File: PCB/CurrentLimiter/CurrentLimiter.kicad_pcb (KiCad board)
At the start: 2 copper layers, 24 parts, among them P1 Signals, P2 OpAmp1-4, P3 OpAmp5-8, Q1 Q_PMOS_GSD, Q2 Q_NPN_BEC, Q3 Q_NPN_BEC, Q4 Q_NPN_BEC, U1 LM358

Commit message: Overcurrent protection proto PCB mostly done
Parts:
- P1: footprint Pin_Headers:Pin_Header_Straight_1x06_Pitch2.54mm -> Pin_Headers:Pin_Header_Straight_1x07_Pitch2.54mm
- moved D1 47.0 mm to (152.0, 129.5), turned to 180 degrees
- moved R6 46.3 mm to (145.4, 115.0), turned to 270 degrees
- moved R5 45.4 mm to (146.7, 128.3), turned to 180 degrees
- moved Q4 42.4 mm to (142.9, 120.7), turned to 90 degrees
- moved R4 35.7 mm to (151.8, 127.0), turned to 180 degrees
- moved R11 32.4 mm to (170.1, 116.8), turned to 180 degrees
- moved R1 30.4 mm to (163.3, 128.6), turned to 180 degrees
- moved W2 30.0 mm to (142.2, 114.9)
- moved R3 29.7 mm to (146.6, 125.1), turned to 180 degrees
- moved R2 28.8 mm to (151.8, 123.8), turned to 180 degrees
- moved R9 28.0 mm to (168.9, 113.0), turned to 90 degrees
- moved P1 26.0 mm to (155.6, 132.7), turned to 90 degrees
- moved Q2 24.2 mm to (157.7, 128.9)
- moved W1 23.2 mm to (158.1, 125.1)
- moved Q3 22.3 mm to (146.4, 120.7), turned to 270 degrees
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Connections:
- P1 pad 1: +12V -> Vref
- P1 pad 3: Vref -> GND
- P1 pad 4: V- -> +12V
- P1 pad 5: V+ -> Vout
- P1 pad 6: GND -> V+
- Q1 pad 3: Net-(Q1-Pad3) -> Vout
- R2 pad 1: Net-(Q1-Pad3) -> Vout
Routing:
- net GND: track 0.00 -> 73.1 mm, vias 0 -> 2
- net Vref: track 4.25 -> 60.3 mm
- net +12V: track 4.91 -> 34.6 mm
- net Vout: track 0.00 -> 23.2 mm
- net /Vbase: track 0.00 -> 22.4 mm
- net V-: track 0.00 -> 18.4 mm
- net V+: track 0.00 -> 16.1 mm
- net ON: track 0.00 -> 13.3 mm
- net /Vdiff: track 7.32 -> 20.1 mm
- net /OC_signal: track 4.77 -> 15.8 mm
- net Net-(Q4-Pad1): track 0.00 -> 9.09 mm
- net Net-(Q3-Pad1): track 0.00 -> 7.66 mm
- net /OpB+: track 4.44 -> 10.7 mm
- net /OpB-: track 3.91 -> 10.1 mm
- net Net-(Q1-Pad1): track 0.00 -> 5.97 mm
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- added copper zone on F.Cu, net (none)
- added copper zone on F.Cu, net GND
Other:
- board outline added: 39 x 28 mm
- net class Default: via_dia 0.6 -> 2; via_drill 0.4 -> 1
- net class Power added: clearance 0.5, trace_width 1, via_dia 2, via_drill 1
- board text added: "OC Prot RG'17"
- board text added: "v1.0"

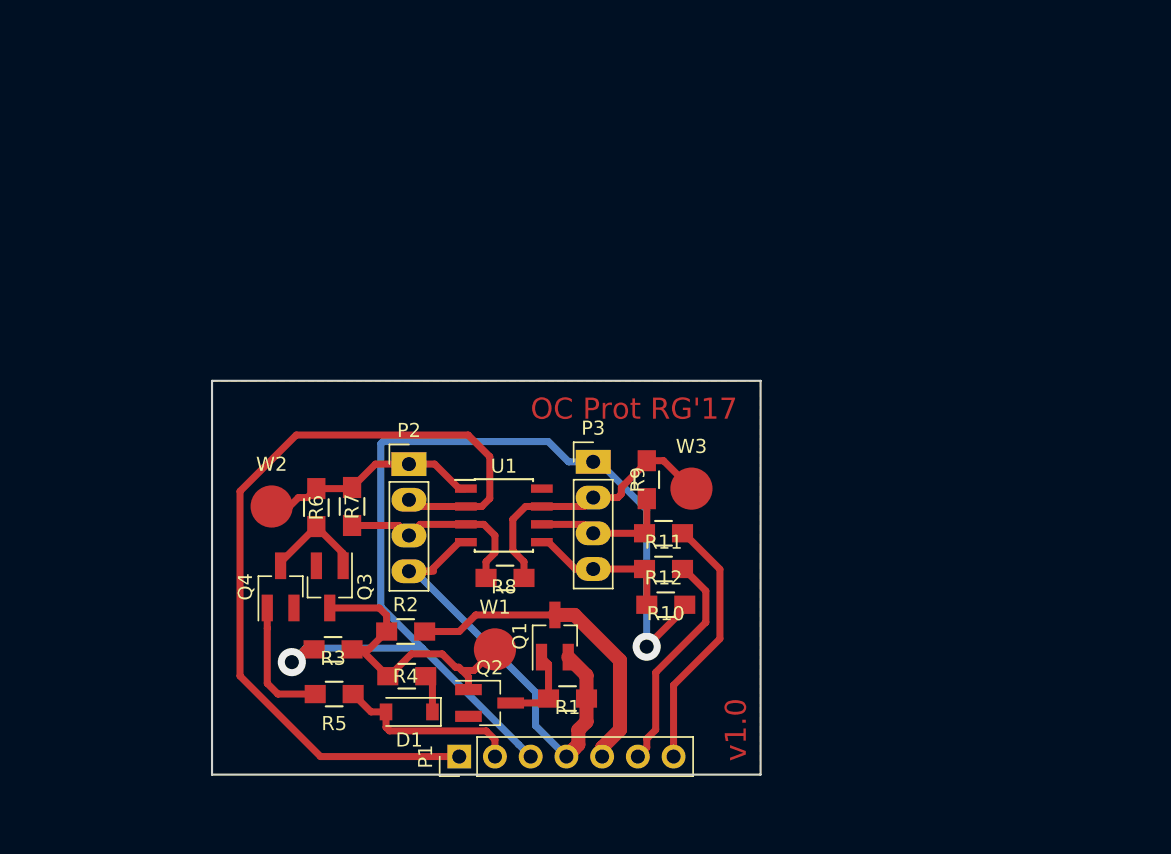
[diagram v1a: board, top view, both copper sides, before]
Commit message: Some minor cleanups for OC proto PCB. Added OPAmp daughter board PCB
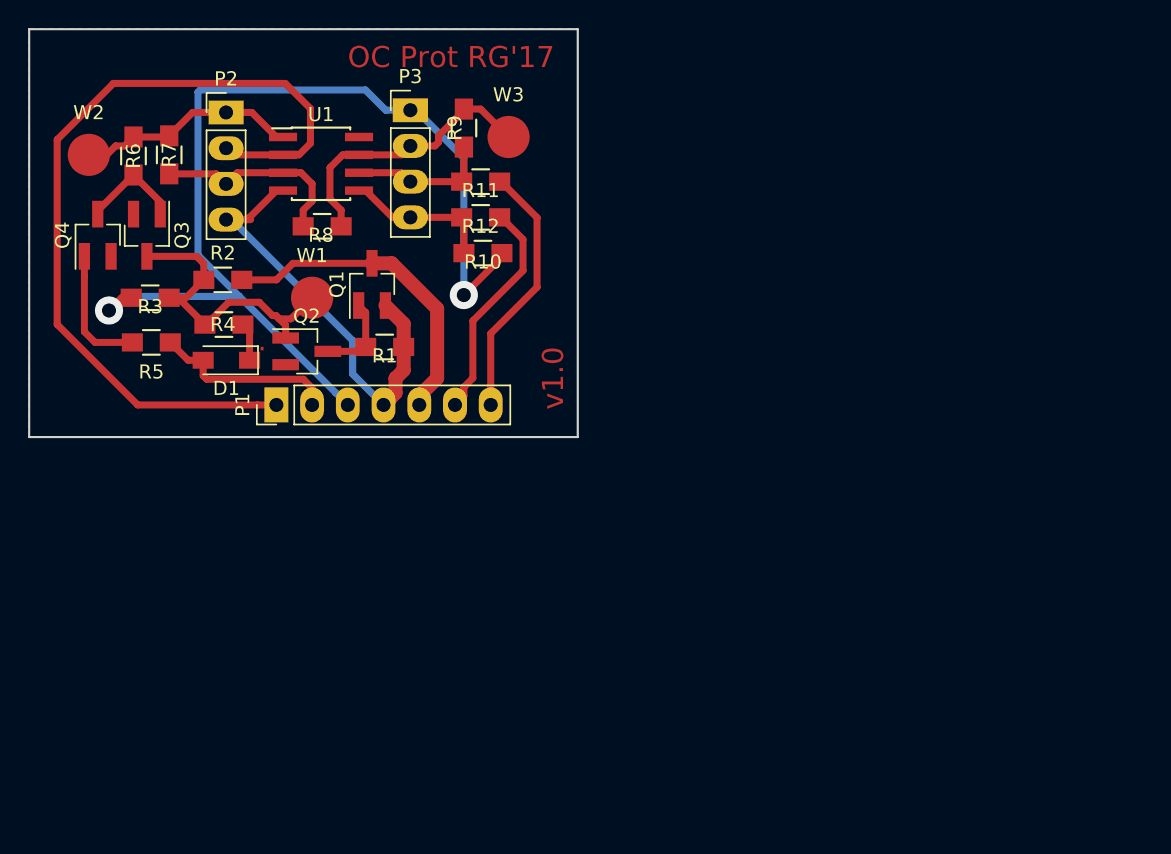
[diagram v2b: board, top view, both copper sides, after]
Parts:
- moved R1 28.2 mm to (150.3, 103.6)
- moved R5 28.2 mm to (133.7, 103.3)
- moved P1 28.2 mm to (142.6, 107.7)
- moved P2 28.2 mm to (139.0, 86.9)
- moved P3 28.2 mm to (152.1, 86.8)
- moved Q1 28.2 mm to (149.4, 99.1)
- moved Q2 28.2 mm to (144.7, 103.9)
- moved Q3 28.2 mm to (133.4, 95.7)
- moved Q4 28.2 mm to (129.9, 95.7)
- moved R10 28.2 mm to (157.3, 96.9)
- moved R11 28.2 mm to (157.1, 91.8)
- moved R12 28.2 mm to (157.1, 94.4)
- moved R2 28.2 mm to (138.8, 98.8)
- moved R3 28.2 mm to (133.6, 100.1)
- moved R4 28.2 mm to (138.8, 102.0)
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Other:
- board size 39 x 28 mm -> 39 x 29 mm
- board text added: "."
